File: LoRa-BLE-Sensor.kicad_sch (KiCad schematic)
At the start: 120 parts, among them J1 SHF-105-01-X-D-SM, J2 Battery_Cell, J3 Conn_01x06_Socket, J4 Screw_Terminal_01x04, J5 Screw_Terminal_01x06, J6 Screw_Terminal_01x06, J7 Conn_01x10_Pin, Q1 DMN67D7L, Q10 SQ2389ES, Q11 DMN62D0UDW-7, Q12 DMN62D0UDW-7, Q13 SQ2389ES, Q2 DMN67D7L, Q3 DMN67D7L, Q4 DMN67D7L, Q5 DMN67D7L, Q6 DMN67D7L, Q7 DMN67D7L, Q8 DMN67D7L, Q9 SQ2389ES, SW1 SW_Push, SW2 SW_Push, SW3 SW_Push, U1 RAK4630, U2 NPM1300-QEAA-R, U3 TLV61046ADBVR, U4 TLV61046ADBVR, U5 TLV61046ADBVR

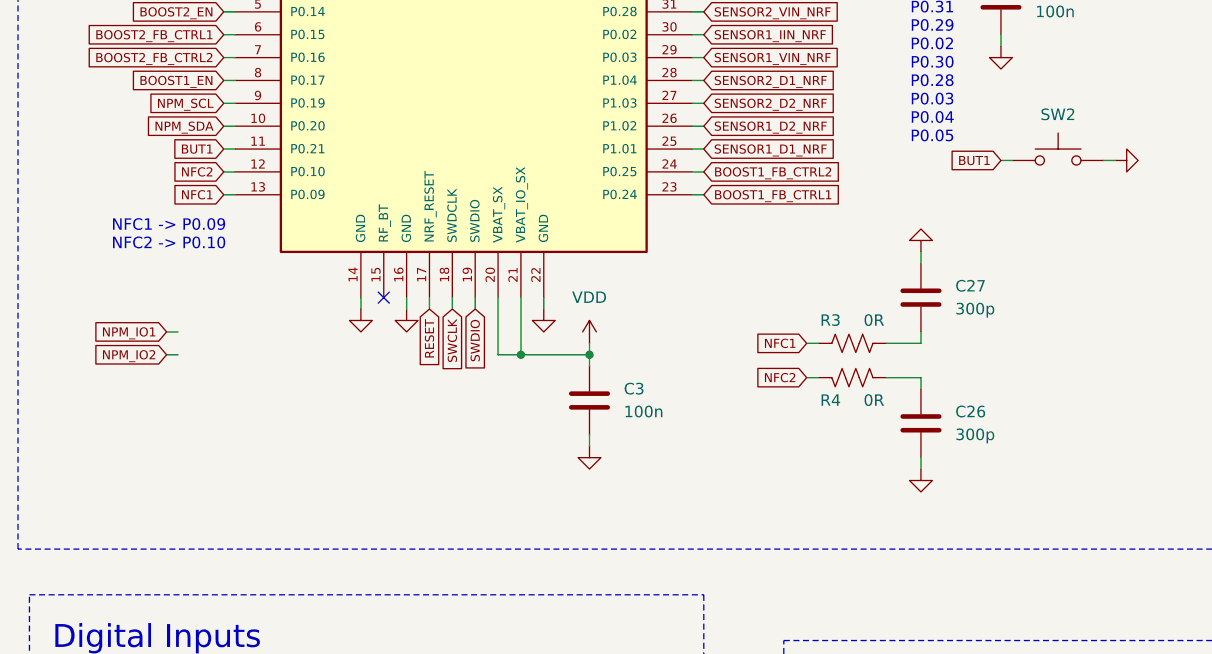
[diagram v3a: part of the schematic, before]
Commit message: NFC antenna route + connector
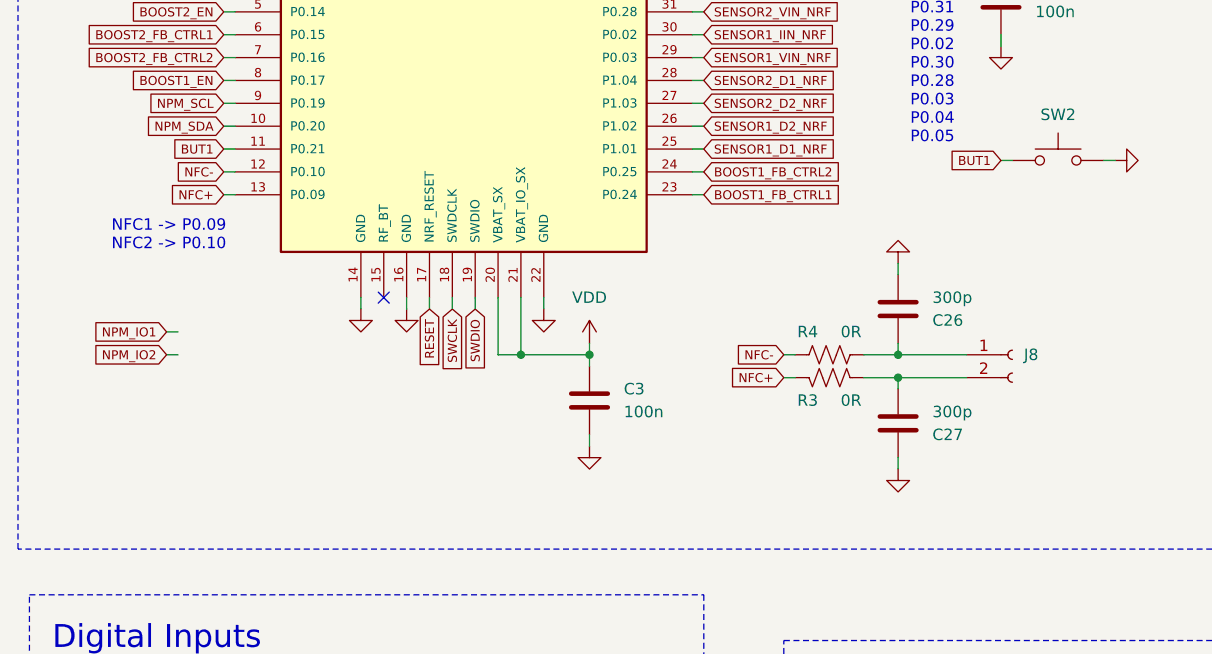
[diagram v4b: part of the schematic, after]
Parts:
- added J8: Conn_01x02_Socket, User_Connectors:JST_ACH_BM02B-ACHSS-GAN-ETF_1x02-1MP_P1.20mm_Vertical, symbol Connector:Conn_01x02_Socket
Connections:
- net at C27.1, R3.2: now also J8.2 (Pin_2)
- net at C26.1, R4.2: now also J8.1 (Pin_1)
- net NFC1 renamed NFC+
- net NFC2 renamed NFC-
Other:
- moved on the sheet: C26, C27, R3, R4

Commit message: mounting holes + routing
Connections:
- net VOUT_SENSOR1 is gone; now on net SENSOR1_PWR: Q3.1 (G), Q4.1 (G), R5.1, R6.1
- net VOUT_SENSOR2 is gone; now on net SENSOR2_PWR: Q7.1 (G), Q8.1 (G), R13.1, R14.1
- net NFC_OUT+: now reaches C27.1, J8.2 (Pin_2), R3.2
- net NFC_OUT-: now reaches C26.1, J8.1 (Pin_1), R4.2
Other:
- moved on the sheet: J8

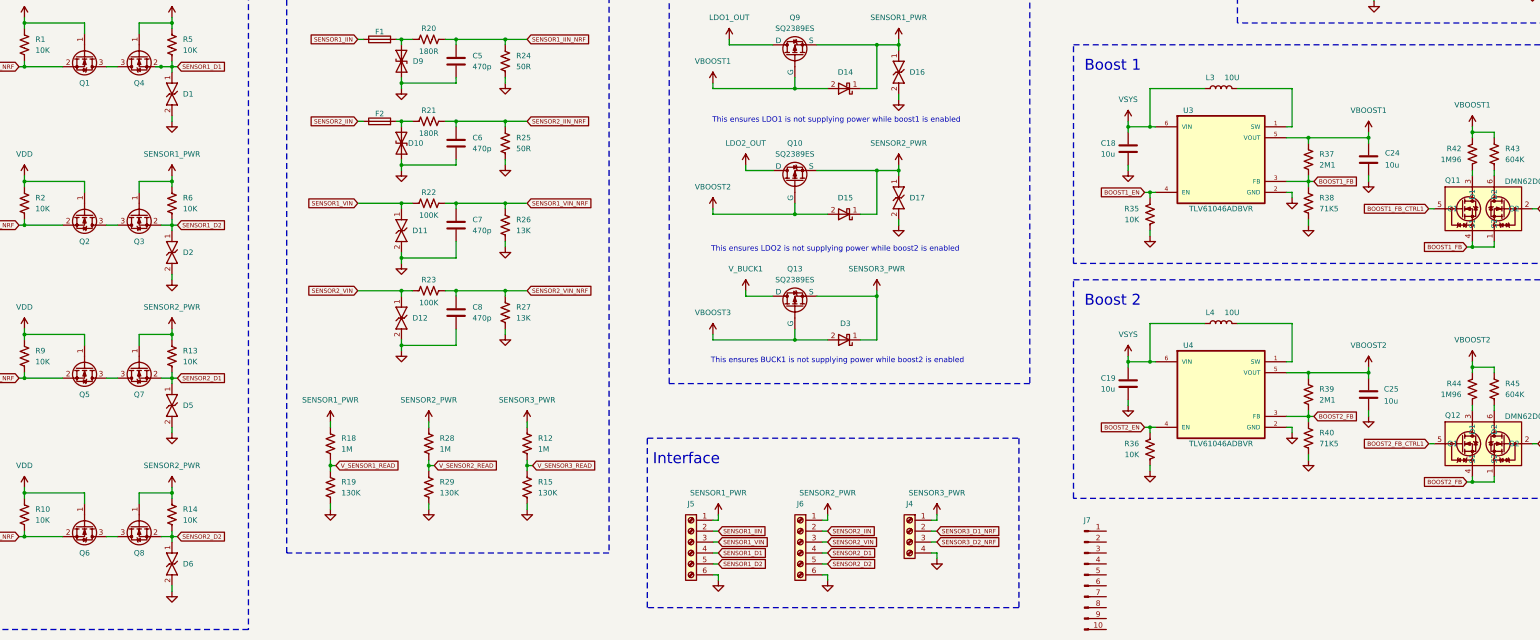
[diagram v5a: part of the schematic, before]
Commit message: all tracks routed and DRC passed
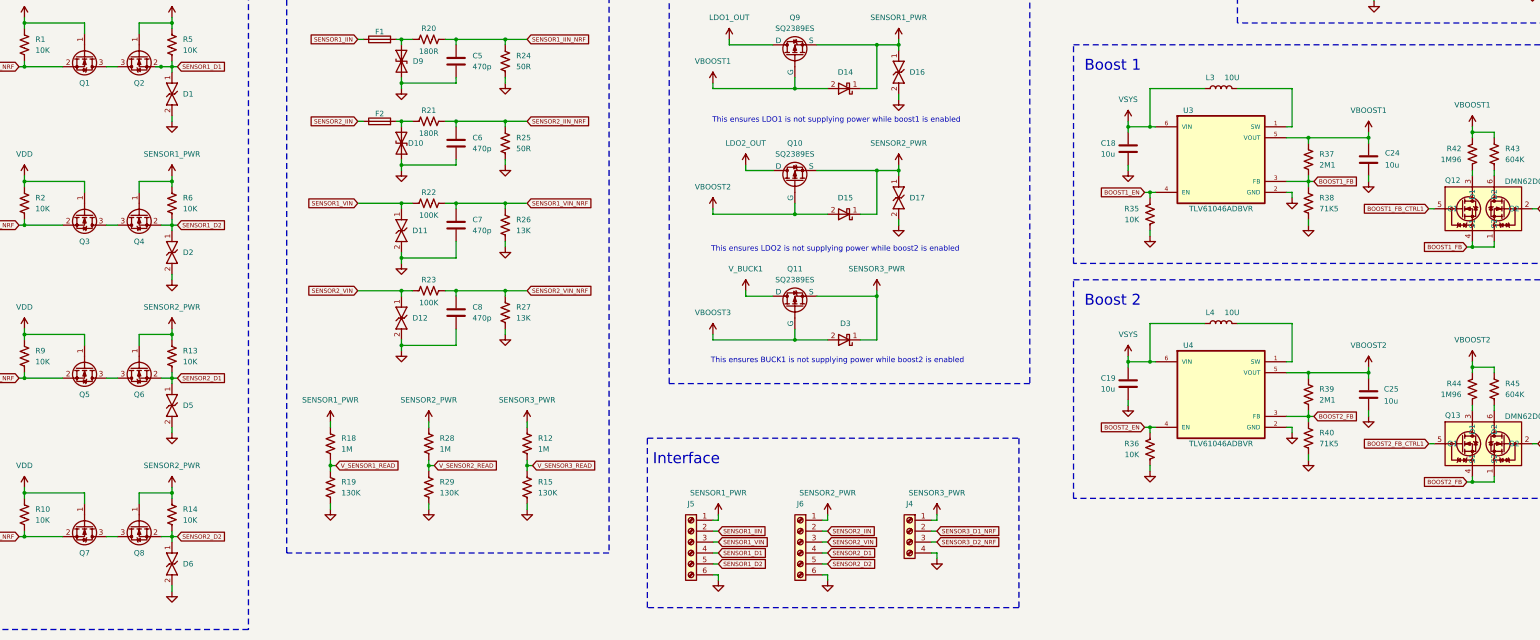
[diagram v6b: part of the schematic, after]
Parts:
- removed J7: Conn_01x10_Pin, Connector_PinHeader_2.54mm:PinHeader_1x10_P2.54mm_Vertical, symbol Connector:Conn_01x10_Pin
- renumbered Q13 to Q11, Q11 to Q12, Q12 to Q13, Q4 to Q2, Q2 to Q3, Q3 to Q4, Q7 to Q6, Q6 to Q7
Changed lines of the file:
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@@
 		(on_board yes)
 		(dnp no)
-		(property "Reference" "Q7"
+		(property "Reference" "Q6"
 			(at 68.58 238.76 90)
 			(effects
@@
 			(project "LoRa-BLE-Sensor"
 				(path "/cc7ac87f-f524-46b8-b856-a8c437fb3dfe"
-					(reference "Q7")
+					(reference "Q6")
 					(unit 1)
 				)
@@
 	)
 	(symbol
-		(lib_id "Connector:Conn_01x10_Pin")
-		(at 288.29 280.67 0)
-		(unit 1)
-		(exclude_from_sim no)
-		(in_bom yes)
-		(on_board yes)
-		(dnp no)
-		(fields_autoplaced yes)
-		(property "Reference" "J7"
-			(at 288.925 267.97 0)
-			(effects
-				(font
-					(size 1.27 1.27)
-				)
-			)
-		)
-		(property "Value" "Conn_01x10_Pin"
-			(at 288.925 267.97 0)
-			(effects
-				(font
-					(size 1.27 1.27)
-				)
-				(hide yes)
-			)
-		)
-		(property "Footprint" "Connector_PinHeader_2.54mm:PinHeader_1x10_P2.54mm_Vertical"
-			(at 288.29 280.67 0)
-			(effects
-				(font
-					(size 1.27 1.27)
-				)
-				(hide yes)
-			)
-		)
-		(property "Datasheet" "~"
-			(at 288.29 280.67 0)
-			(effects
-				(font
-					(size 1.27 1.27)
-				)
-				(hide yes)
-			)
-		)
-		(property "Description" "Generic connector, single row, 01x10, script generated"
-			(at 288.29 280.67 0)
-			(effects
-				(font
-					(size 1.27 1.27)
-				)
-				(hide yes)
-			)
-		)
-		(pin "8"
-		)
-		(pin "4"
-		)
-		(pin "6"
-		)
-		(pin "10"
-		)
-		(pin "5"
-		)
-		(pin "3"
-		)
-		(pin "9"
-		)
-		(pin "7"
-		)
-		(pin "2"
-		)
-		(pin "1"
-		)
-		(instances
-			(project ""
-				(path "/cc7ac87f-f524-46b8-b856-a8c437fb3dfe"
-					(reference "J7")
-					(unit 1)
-				)
-			)
-		)
-	)
-	(symbol
 		(lib_id "power:GND")
 		(at 76.2 46.99 180)
@@
 		(on_board yes)
 		(dnp no)
-		(property "Reference" "Q3"
+		(property "Reference" "Q4"
 			(at 68.58 203.2 90)
 			(effects
@@
 			(project "LoRa-BLE-Sensor"
 				(path "/cc7ac87f-f524-46b8-b856-a8c437fb3dfe"
-					(reference "Q3")
+					(reference "Q4")
 					(unit 1)
 				)
@@
 		(dnp no)
 		(fields_autoplaced yes)
-		(property "Reference" "Q13"
+		(property "Reference" "Q11"
 			(at 220.98 209.55 90)
 			(effects
@@
 			(project "LoRa-BLE-Sensor"
 				(path "/cc7ac87f-f524-46b8-b856-a8c437fb3dfe"
-					(reference "Q13")
+					(reference "Q11")
 					(unit 1)
 				)
@@
 		(on_board yes)
 		(dnp no)
-		(property "Reference" "Q11"
+		(property "Reference" "Q12"
 			(at 373.888 188.976 0)
 			(effects
@@
 			(project ""
 				(path "/cc7ac87f-f524-46b8-b856-a8c437fb3dfe"
-					(reference "Q11")
+					(reference "Q12")
 					(unit 1)
 				)
@@
 		(on_board yes)
 		(dnp no)
-		(property "Reference" "Q2"
+		(property "Reference" "Q3"
 			(at 55.88 203.2 90)
 			(effects
@@
 			(project "LoRa-BLE_Sensor_V0.1"
 				(path "/cc7ac87f-f524-46b8-b856-a8c437fb3dfe"
-					(reference "Q2")
+					(reference "Q3")
 					(unit 1)
 				)
@@
 		(on_board yes)
 		(dnp no)
-		(property "Reference" "Q6"
+		(property "Reference" "Q7"
 			(at 55.88 275.59 90)
 			(effects
@@
 			(project "LoRa-BLE_Sensor_V0.1"
 				(path "/cc7ac87f-f524-46b8-b856-a8c437fb3dfe"
-					(reference "Q6")
+					(reference "Q7")
 					(unit 1)
 				)
@@
 		(on_board yes)
 		(dnp no)
-		(property "Reference" "Q4"
+		(property "Reference" "Q2"
 			(at 68.58 166.37 90)
 			(effects
@@
 			(project "LoRa-BLE-Sensor"
 				(path "/cc7ac87f-f524-46b8-b856-a8c437fb3dfe"
-					(reference "Q4")
+					(reference "Q2")
 					(unit 1)
 				)
@@
 		(on_board yes)
 		(dnp no)
-		(property "Reference" "Q12"
+		(property "Reference" "Q13"
 			(at 373.888 243.586 0)
 			(effects
@@
 			(project "LoRa-BLE_Sensor_V0.1"
 				(path "/cc7ac87f-f524-46b8-b856-a8c437fb3dfe"
-					(reference "Q12")
+					(reference "Q13")
 					(unit 1)
 				)

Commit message: finished renaming and routing
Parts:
- added J8, J9: Conn_01x04_Pin, Connector_PinHeader_2.54mm:PinHeader_1x04_P2.54mm_Vertical, symbol Connector:Conn_01x04_Pin
- renumbered C23 to C10, C16 to C11, C20 to C12, C22 to C13, C13 to C14, C14 to C15, C12 to C16, C15 to C17, C17 to C18, C21 to C19, C5 to C20, C6 to C21, C7 to C22, C8 to C23, C18 to C24, C24 to C25, C19 to C26, C25 to C27, C26 to C5, C27 to C6, C10 to C7, C9 to C8, C11 to C9, D13 to D1, D12 to D10, D14 to D11, D16 to D12, D15 to D13, D17 to D14, D3 to D15, D7 to D16, D20 to D2, D1 to D3, D2 to D4, D9 to D7, D10 to D8, D11 to D9, J8 to J2, J2 to J3, J3 to J4, J4 to J7, R4 to R1, R13 to R10, R10 to R11, R14 to R12, R20 to R13, R24 to R14, R21 to R15, R25 to R16, R22 to R17, R26 to R18, R23 to R19, R3 to R2, R27 to R20, R18 to R21, R19 to R22, R28 to R23, R29 to R24, R12 to R25, R15 to R26, R35 to R27, R37 to R28, R38 to R29, R17 to R3, R42 to R30, R43 to R31, R36 to R32, R39 to R33, R40 to R34, R44 to R35, R45 to R36, R7 to R37, R8 to R38, R11 to R39, R30 to R4, R1 to R5, R5 to R6, R2 to R7, R6 to R8
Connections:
- net GND: now also J8.4 (Pin_4), J9.4 (Pin_4)
- net SENSOR1_D1_NRF: now also J8.3 (Pin_3)
- net SENSOR1_D2_NRF: now also J8.2 (Pin_2)
- net SENSOR2_D1_NRF: now also J9.2 (Pin_2)
- net SENSOR2_D2_NRF: now also J9.3 (Pin_3)
- net VDD: now also J8.1 (Pin_1), J9.1 (Pin_1)
- net NPM_IO1: no longer names the net of U2.8 (GPIO1)
- net NPM_IO2: no longer names the net of U2.9 (GPIO2)
- no-connect marks 7 -> 9
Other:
- moved on the sheet: C10, C5

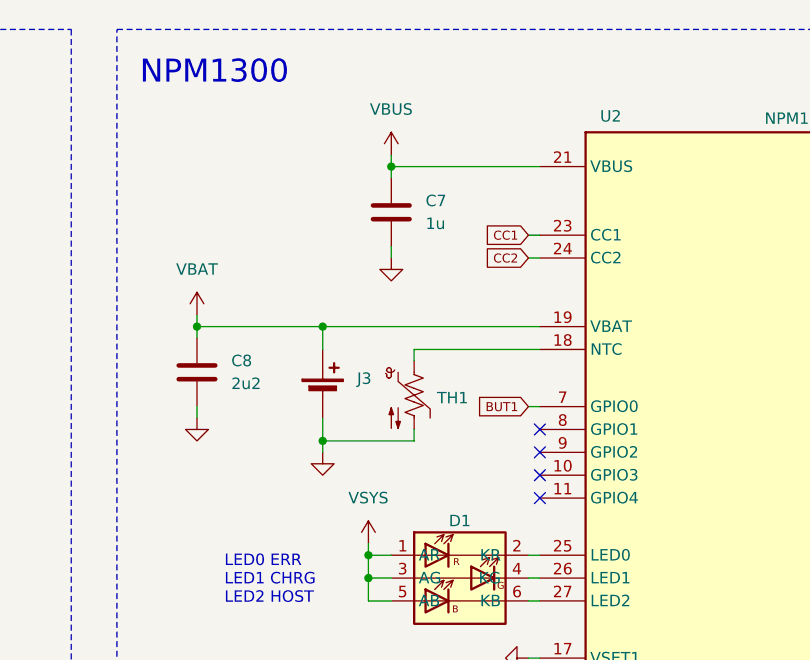
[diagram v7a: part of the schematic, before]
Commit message: replaced battery connectors
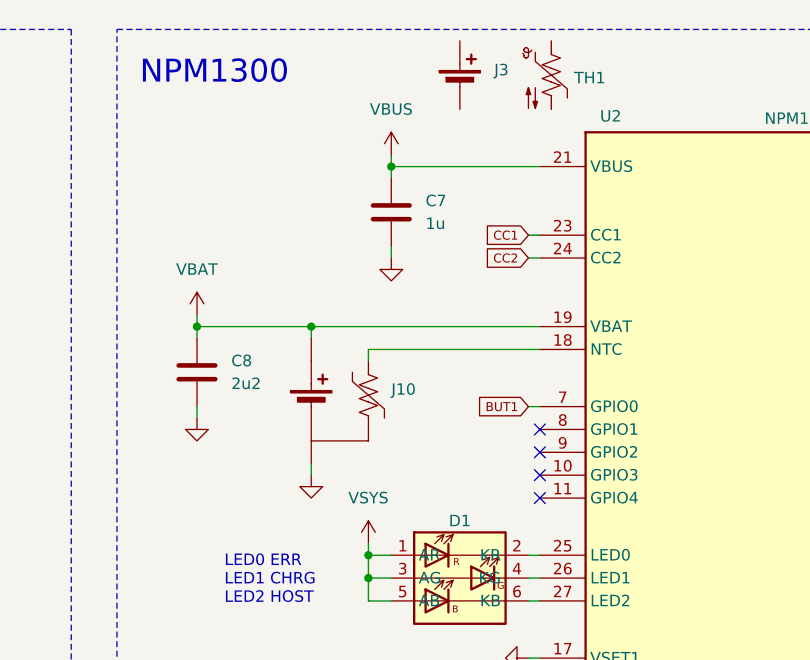
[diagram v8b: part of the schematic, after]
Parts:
- added J10: Battery_with_NTC, Connector_JST:JST_SH_BM03B-SRSS-TB_1x03-1MP_P1.00mm_Vertical, symbol User_Connectors:Battery_with_NTC
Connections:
- net GND: now also J10.3 (-); no longer J3.2 (-), TH1.2
- net VBAT: now also J10.1 (+); no longer J3.1 (+)
- net at U2.18 (NTC): now also J10.2 (NTC); no longer TH1.1
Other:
- moved on the sheet: J3, TH1
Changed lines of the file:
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@@
 	)
 	(junction
+		(at 180.34 50.8)
+		(diameter 0)
+		(color 0 0 0 0)
+	)
+	(junction
 		(at 153.67 156.21)
 		(diameter 0)
@@
 	)
 	(junction
-		(at 181.61 63.5)
-		(diameter 0)
-		(color 0 0 0 0)
-	)
-	(junction
 		(at 34.29 38.1)
 		(diameter 0)
@@
 	)
 	(junction
-		(at 181.61 50.8)
-		(diameter 0)
-		(color 0 0 0 0)
-	)
-	(junction
 		(at 240.03 186.69)
 		(diameter 0)
@@
 	(wire
 		(pts
+			(xy 180.34 66.04) (xy 180.34 67.31)
+		)
+		(stroke
+			(width 0)
+			(type default)
+		)
+	)
+	(wire
+		(pts
 			(xy 340.36 44.45) (xy 341.63 44.45)
 		)
@@
 	(wire
 		(pts
-			(xy 191.77 54.61) (xy 191.77 53.34)
-		)
-		(stroke
-			(width 0)
-			(type default)
-		)
-	)
-	(wire
-		(pts
 			(xy 378.46 25.4) (xy 378.46 26.67)
 		)
@@
 	(wire
 		(pts
-			(xy 181.61 53.34) (xy 181.61 50.8)
-		)
-		(stroke
-			(width 0)
-			(type default)
-		)
-	)
-	(wire
-		(pts
 			(xy 303.53 231.14) (xy 304.8 231.14)
 		)
@@
 	(wire
 		(pts
-			(xy 191.77 63.5) (xy 181.61 63.5)
-		)
-		(stroke
-			(width 0)
-			(type default)
-		)
-	)
-	(wire
-		(pts
 			(xy 270.51 72.39) (xy 270.51 71.12)
 		)
@@
 	(wire
 		(pts
-			(xy 191.77 53.34) (xy 205.74 53.34)
-		)
-		(stroke
-			(width 0)
-			(type default)
-		)
-	)
-	(wire
-		(pts
 			(xy 127 86.36) (xy 128.27 86.36)
 		)
@@
 	(wire
 		(pts
-			(xy 167.64 50.8) (xy 181.61 50.8)
+			(xy 167.64 50.8) (xy 180.34 50.8)
 		)
 		(stroke
@@
 	(wire
 		(pts
+			(xy 180.34 50.8) (xy 205.74 50.8)
+		)
+		(stroke
+			(width 0)
+			(type default)
+		)
+	)
+	(wire
+		(pts
 			(xy 209.55 185.42) (xy 209.55 186.69)
 		)
@@
 	(wire
 		(pts
+			(xy 186.69 53.34) (xy 186.69 54.61)
+		)
+		(stroke
+			(width 0)
+			(type default)
+		)
+	)
+	(wire
+		(pts
 			(xy 127 31.75) (xy 128.27 31.75)
 		)
@@
 	(wire
 		(pts
-			(xy 191.77 62.23) (xy 191.77 63.5)
+			(xy 285.75 52.07) (xy 285.75 53.34)
 		)
 		(stroke
@@
 	(wire
 		(pts
-			(xy 285.75 52.07) (xy 285.75 53.34)
+			(xy 186.69 53.34) (xy 205.74 53.34)
 		)
 		(stroke
@@
 	(wire
 		(pts
-			(xy 181.61 60.96) (xy 181.61 63.5)
-		)
-		(stroke
-			(width 0)
-			(type default)
-		)
-	)
-	(wire
-		(pts
 			(xy 158.75 264.16) (xy 158.75 265.43)
 		)
@@
 	(wire
 		(pts
+			(xy 180.34 50.8) (xy 180.34 52.07)
+		)
+		(stroke
+			(width 0)
+			(type default)
+		)
+	)
+	(wire
+		(pts
 			(xy 205.74 156.21) (xy 205.74 157.48)
 		)
@@
 	(wire
 		(pts
-			(xy 181.61 64.77) (xy 181.61 63.5)
-		)
-		(stroke
-			(width 0)
-			(type default)
-		)
-	)
-	(wire
-		(pts
 			(xy 204.47 102.87) (xy 205.74 102.87)
 		)
@@
 	(wire
 		(pts
-			(xy 181.61 50.8) (xy 205.74 50.8)
-		)
-		(stroke
-			(width 0)
-			(type default)
-		)
-	)
-	(wire
-		(pts
 			(xy 201.93 166.37) (xy 201.93 167.64)
 		)
@@
 	(symbol
 		(lib_id "Device:Thermistor_NTC_US")
-		(at 191.77 58.42 0)
+		(at 207.01 22.86 0)
 		(unit 1)
 		(exclude_from_sim no)
@@
 		(fields_autoplaced yes)
 		(property "Reference" "TH1"
-			(at 194.31 58.7374 0)
+			(at 209.55 23.1774 0)
 			(effects
 				(font
@@
 		)
 		(property "Value" "10K"
-			(at 194.31 60.0074 0)
+			(at 209.55 24.4474 0)
 			(effects
 				(font
@@
 		)
 		(property "Footprint" "Resistor_THT:R_Axial_DIN0204_L3.6mm_D1.6mm_P1.90mm_Vertical"
-			(at 191.77 57.15 0)
+			(at 207.01 21.59 0)
 			(effects
 				(font
@@
 		)
 		(property "Datasheet" "~"
-			(at 191.77 57.15 0)
+			(at 207.01 21.59 0)
 			(effects
 				(font
@@
 		)
 		(property "Description" "Temperature dependent resistor, negative temperature coefficient, US symbol"
-			(at 191.77 58.42 0)
+			(at 207.01 22.86 0)
 			(effects
 				(font
@@
 	(symbol
 		(lib_id "Device:Battery_Cell")
-		(at 181.61 58.42 0)
+		(at 196.85 24.13 0)
 		(unit 1)
 		(exclude_from_sim no)
@@
 		(fields_autoplaced yes)
 		(property "Reference" "J3"
-			(at 185.42 56.5784 0)
+			(at 200.66 22.2884 0)
 			(effects
 				(font
@@
 		)
 		(property "Value" "Battery_Cell"
-			(at 185.42 57.8484 0)
+			(at 200.66 23.5584 0)
 			(effects
 				(font
@@
 		)
 		(property "Footprint" "User_Connectors:18650_CLIP_PROTECTED"
-			(at 181.61 56.896 90)
+			(at 196.85 22.606 90)
 			(effects
 				(font
@@
 		)
 		(property "Datasheet" "~"
-			(at 181.61 56.896 90)
+			(at 196.85 22.606 90)
 			(effects
 				(font
@@
 		)
 		(property "Description" "Single-cell battery"
-			(at 181.61 58.42 0)
+			(at 196.85 24.13 0)
 			(effects
 				(font
@@
 	)
 	(symbol
+		(lib_id "User_Connectors:Battery_with_NTC")
+		(at 180.34 58.42 0)
+		(unit 1)
+		(exclude_from_sim no)
+		(in_bom yes)
+		(on_board yes)
+		(dnp no)
+		(property "Reference" "J10"
+			(at 189.23 57.7849 0)
+			(effects
+				(font
+					(size 1.27 1.27)
+				)
+				(justify left)
+			)
+		)
+		(property "Value" "Battery_with_NTC"
+			(at 189.23 60.3249 0)
+			(effects
+				(font
+					(size 1.27 1.27)
+				)
+				(justify left)
+				(hide yes)
+			)
+		)
+		(property "Footprint" "Connector_JST:JST_SH_BM03B-SRSS-TB_1x03-1MP_P1.00mm_Vertical"
+			(at 180.34 56.896 90)
+			(effects
+				(font
+					(size 1.27 1.27)
+				)
+				(hide yes)
+			)
+		)
+		(property "Datasheet" "~"
+			(at 180.34 56.896 90)
+			(effects
+				(font
+					(size 1.27 1.27)
+				)
+				(hide yes)
+			)
+		)
+		(property "Description" "Battery Connector with NTC"
+			(at 156.718 56.642 0)
+			(effects
+				(font
+					(size 1.27 1.27)
+				)
+				(hide yes)
+			)
+		)
+		(pin "3"
+		)
+		(pin "2"
+		)
+		(pin "1"
+		)
+		(instances
+			(project ""
+				(path "/cc7ac87f-f524-46b8-b856-a8c437fb3dfe"
+					(reference "J10")
+					(unit 1)
+				)
+			)
+		)
+	)
+	(symbol
 		(lib_id "Device:R_US")
 		(at 378.46 182.88 0)
@@
 	(symbol
 		(lib_id "power:GND")
-		(at 181.61 64.77 0)
+		(at 180.34 67.31 0)
 		(unit 1)
 		(exclude_from_sim no)
@@
 		(fields_autoplaced yes)
 		(property "Reference" "#PWR058"
-			(at 181.61 71.12 0)
+			(at 180.34 73.66 0)
 			(effects
 				(font
@@
 		)
 		(property "Value" "GND"
-			(at 181.61 69.85 0)
+			(at 180.34 72.39 0)
 			(effects
 				(font
@@
 		)
 		(property "Footprint" ""
-			(at 181.61 64.77 0)
+			(at 180.34 67.31 0)
 			(effects
 				(font
@@
 		)
 		(property "Datasheet" ""
-			(at 181.61 64.77 0)
+			(at 180.34 67.31 0)
 			(effects
 				(font
@@
 		)
 		(property "Description" "Power symbol creates a global label with name \"GND\" , ground"
-			(at 181.61 64.77 0)
+			(at 180.34 67.31 0)
 			(effects
 				(font
